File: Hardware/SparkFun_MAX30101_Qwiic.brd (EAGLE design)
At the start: 25.4 x 25.4 mm, 57 parts, among them J1 PTH, J3 QWIIC_RA, J5 QWIIC_RA, Q6 20V/0.2A/8MHz/1.2Ω/1Vth, Q8 20V/0.2A/8MHz/1.2Ω/1Vth, U1 1.8V/100mA, U2 MAX30101

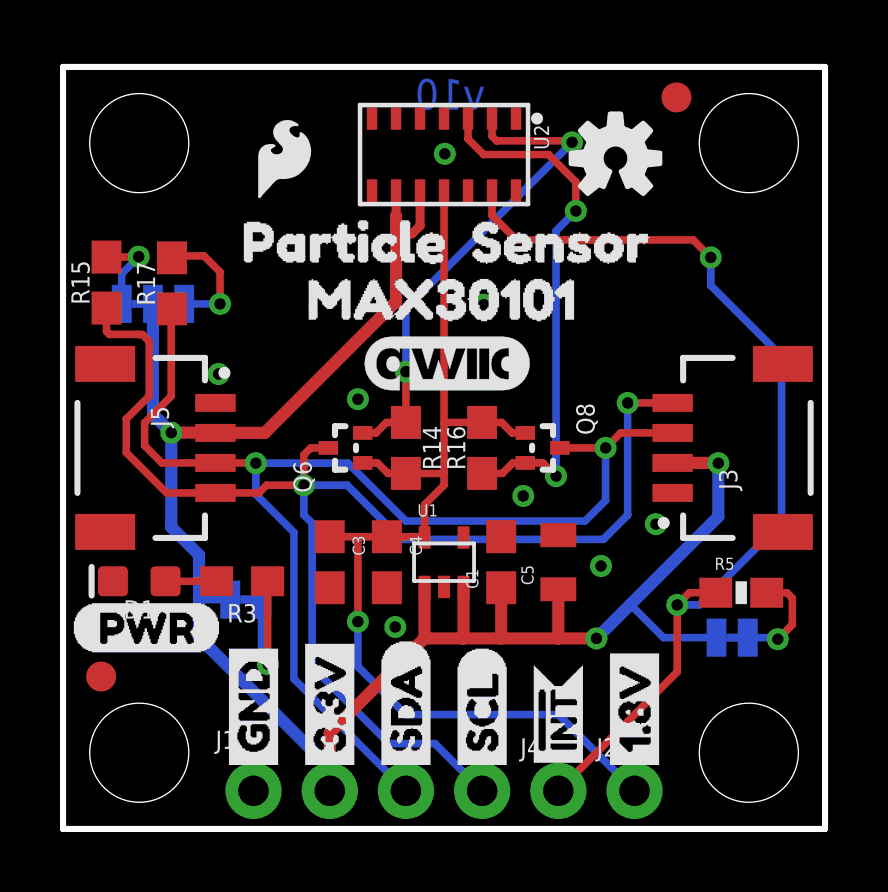
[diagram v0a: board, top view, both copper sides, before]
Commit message: Qwiic logo in SCH and sch cleanup
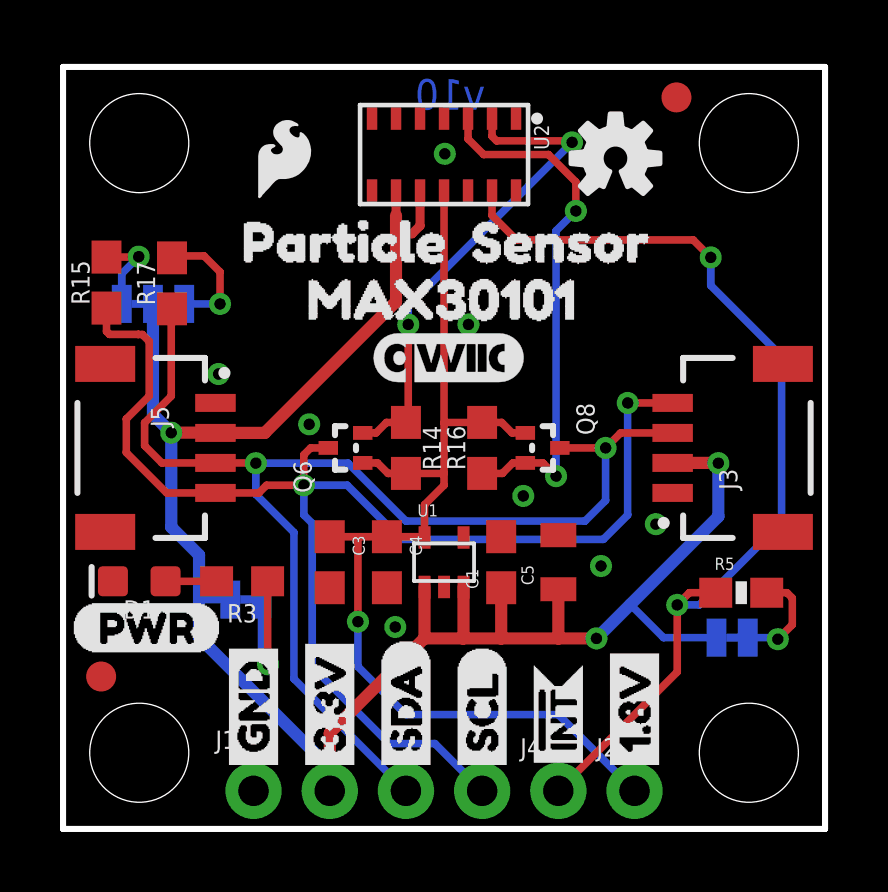
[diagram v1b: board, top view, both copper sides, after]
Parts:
- removed U$15: (no value), SparkFun-Aesthetics:QWIIC_5.5MM
- added LOGO3: QWIIC_LOGO_5MM, SparkFun-Aesthetics:QWIIC_5MM
- moved LOGO1 0.43 mm to (13.3, 17.8)
- moved U$17 0.31 mm to (20.8, 15.9)
- moved U$18 0.30 mm to (13.4, 16.0)
- moved U$24 0.18 mm to (18.7, 14.1)
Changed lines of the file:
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@@
 <grid distance="0.05" unitdist="inch" unit="inch" style="lines" multiple="1" display="yes" altdistance="0.001" altunitdist="inch" altunit="inch"/>
 <layers>
-<layer number="1" name="Top" color="4" fill="1" visible="yes" active="yes"/>
+<layer number="1" name="Top" color="4" fill="1" visible="no" active="yes"/>
 <layer number="2" name="Route2" color="1" fill="3" visible="no" active="no"/>
 <layer number="3" name="Route3" color="4" fill="3" visible="no" active="no"/>
@@
 <layer number="14" name="Route14" color="1" fill="6" visible="no" active="no"/>
 <layer number="15" name="Route15" color="4" fill="6" visible="no" active="no"/>
-<layer number="16" name="Bottom" color="1" fill="1" visible="yes" active="yes"/>
-<layer number="17" name="Pads" color="2" fill="1" visible="yes" active="yes"/>
+<layer number="16" name="Bottom" color="1" fill="1" visible="no" active="yes"/>
+<layer number="17" name="Pads" color="2" fill="1" visible="no" active="yes"/>
 <layer number="18" name="Vias" color="2" fill="1" visible="yes" active="yes"/>
-<layer number="19" name="Unrouted" color="6" fill="1" visible="yes" active="yes"/>
-<layer number="20" name="Dimension" color="15" fill="1" visible="yes" active="yes"/>
-<layer number="21" name="tPlace" color="16" fill="1" visible="yes" active="yes"/>
+<layer number="19" name="Unrouted" color="6" fill="1" visible="no" active="yes"/>
+<layer number="20" name="Dimension" color="15" fill="1" visible="no" active="yes"/>
+<layer number="21" name="tPlace" color="16" fill="1" visible="no" active="yes"/>
 <layer number="22" name="bPlace" color="14" fill="1" visible="yes" active="yes"/>
-<layer number="23" name="tOrigins" color="15" fill="1" visible="yes" active="yes"/>
+<layer number="23" name="tOrigins" color="15" fill="1" visible="no" active="yes"/>
 <layer number="24" name="bOrigins" color="15" fill="1" visible="yes" active="yes"/>
 <layer number="25" name="tNames" color="7" fill="1" visible="no" active="yes"/>
@@
 <layer number="43" name="vRestrict" color="2" fill="10" visible="no" active="yes"/>
 <layer number="44" name="Drills" color="7" fill="1" visible="no" active="yes"/>
-<layer number="45" name="Holes" color="7" fill="1" visible="yes" active="yes"/>
+<layer number="45" name="Holes" color="7" fill="1" visible="no" active="yes"/>
 <layer number="46" name="Milling" color="3" fill="1" visible="no" active="yes"/>
 <layer number="47" name="Measures" color="7" fill="1" visible="no" active="yes"/>
 <layer number="48" name="Document" color="7" fill="1" visible="no" active="yes"/>
-<layer number="49" name="Reference" color="7" fill="1" visible="yes" active="yes"/>
+<layer number="49" name="Reference" color="7" fill="1" visible="no" active="yes"/>
 <layer number="50" name="dxf" color="7" fill="1" visible="no" active="no"/>
-<layer number="51" name="tDocu" color="6" fill="1" visible="yes" active="yes"/>
+<layer number="51" name="tDocu" color="6" fill="1" visible="no" active="yes"/>
 <layer number="52" name="bDocu" color="7" fill="1" visible="no" active="yes"/>
 <layer number="53" name="tGND_GNDA" color="7" fill="9" visible="no" active="no"/>
@@
 <attribute name="VALUE" x="7.747" y="9.906" size="0.4064" layer="27" font="vector" rot="R270"/>
 </element>
-<element name="LOGO1" library="SparkFun-Aesthetics" package="SFE_LOGO_NAME_FLAME_.1" value="SFE_LOGO_NAME_FLAME.1_INCH" x="13.335" y="18.2626" smashed="yes" rot="MR0"/>
+<element name="LOGO1" library="SparkFun-Aesthetics" package="SFE_LOGO_NAME_FLAME_.1" value="SFE_LOGO_NAME_FLAME.1_INCH" x="13.3096" y="17.8308" smashed="yes" rot="MR0"/>
 <element name="LOGO2" library="SparkFun-Aesthetics" package="OSHW-LOGO-S" value="OSHW-LOGOS" x="18.415" y="22.352" smashed="yes"/>
 <element name="U2" library="SparkFun-Sensors" package="OLGA-14" value="MAX30101" x="12.7" y="22.479" smashed="yes" rot="R270">
@@
 <element name="U$20" library="Labels" package="PWR-()-04" value="" x="0.2794" y="6.7056" smashed="yes"/>
 <element name="U$8" library="buzzard_labels (5)" package="LED0" value="" x="8.4582" y="9.398" smashed="yes" rot="MR0"/>
-<element name="U$15" library="SparkFun-Aesthetics" package="QWIIC_5.5MM" value="" x="12.8016" y="15.5194" smashed="yes"/>
 <element name="JP4" library="SparkFun-Jumpers" package="SMT-JUMPER_3_2-NC_TRACE_SILK" package3d_urn="urn:adsk.eagle:package:39289/1" value="I2C PU" x="2.9972" y="17.5006" smashed="yes" rot="MR0">
 <attribute name="NAME" x="2.9972" y="18.6436" size="0.6096" layer="26" font="vector" ratio="20" rot="MR0" align="bottom-center"/>
@@
 <element name="U$6" library="buzzard_labels (8)" package="1#8V1" value="" x="19.05" y="1.651" smashed="yes" rot="MR90"/>
 <element name="U$16" library="SparkFun-Aesthetics" package="QWIIC_5.5MM" value="" x="13.3604" y="12.192" smashed="yes" rot="MR0"/>
-<element name="U$17" library="buzzard_labels (7)" package="PARTICLE1" value="" x="20.828" y="16.2306" smashed="yes" rot="MR0"/>
-<element name="U$18" library="buzzard_labels (7)" package="SENSOR2" value="" x="13.208" y="16.2306" smashed="yes" rot="MR0"/>
-<element name="U$24" library="buzzard_labels (7)" package="MAX301010" value="" x="18.669" y="14.3256" smashed="yes" rot="MR0"/>
+<element name="U$17" library="buzzard_labels (7)" package="PARTICLE1" value="" x="20.8026" y="15.9258" smashed="yes" rot="MR0"/>
+<element name="U$18" library="buzzard_labels (7)" package="SENSOR2" value="" x="13.3604" y="15.9766" smashed="yes" rot="MR0"/>
+<element name="U$24" library="buzzard_labels (7)" package="MAX301010" value="" x="18.7198" y="14.1478" smashed="yes" rot="MR0"/>
+<element name="LOGO3" library="SparkFun-Aesthetics" package="QWIIC_5MM" value="QWIIC_LOGO_5MM" x="12.827" y="15.7226" smashed="yes"/>
 </elements>
 <signals>
@@
 <via x="5.1816" y="15.1638" extent="1-16" drill="0.381"/>
 <via x="12.7254" y="22.5044" extent="1-16" drill="0.381"/>
-<via x="14.0208" y="17.4752" extent="1-16" drill="0.381"/>
-<via x="9.8298" y="14.3256" extent="1-16" drill="0.381"/>
+<via x="13.5128" y="16.8148" extent="1-16" drill="0.381"/>
+<via x="8.2042" y="13.4874" extent="1-16" drill="0.381"/>
 </signal>
 <signal name="SDA">
@@
 <wire x1="10.4314" y1="13.2" x2="9.99" y2="13.2" width="0.254" layer="1"/>
 <wire x1="10.7814" y1="13.55" x2="10.4314" y2="13.2" width="0.254" layer="1"/>
-<wire x1="11.43" y1="13.55" x2="11.43" y2="15.24" width="0.254" layer="1"/>
-<via x="11.43" y="15.24" extent="1-16" drill="0.381"/>
-<wire x1="11.43" y1="15.24" x2="11.43" y2="17.3482" width="0.254" layer="16"/>
-<wire x1="11.43" y1="17.3482" x2="16.9672" y2="22.8854" width="0.254" layer="16"/>
+<wire x1="11.5062" y1="16.8148" x2="11.5062" y2="13.6262" width="0.254" layer="1"/>
+<wire x1="11.43" y1="13.55" x2="11.5062" y2="13.6262" width="0.254" layer="1"/>
+<via x="11.5062" y="16.8148" extent="1-16" drill="0.381"/>
+<wire x1="11.5062" y1="16.8148" x2="11.5062" y2="17.4244" width="0.254" layer="16"/>
+<wire x1="11.5062" y1="17.4244" x2="16.9672" y2="22.8854" width="0.254" layer="16"/>
 <via x="16.9672" y="22.8854" extent="1-16" drill="0.381"/>
 <wire x1="14.3" y1="23.679" x2="14.3" y2="23.0888" width="0.254" layer="1"/>

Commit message: Added I2C address to bottom silk
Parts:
- added U$15: (no value), buzzard_labels (9):ADR#_0X570
- moved LOGO1 2.56 mm to (12.9, 20.3)
- moved U$17 2.29 mm to (20.6, 18.2)
- moved U$18 2.21 mm to (13.3, 18.2)
- moved U$24 1.87 mm to (18.5, 16.0)
- moved U$16 1.84 mm to (13.0, 14.0)
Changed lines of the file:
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@@
 <grid distance="0.05" unitdist="inch" unit="inch" style="lines" multiple="1" display="yes" altdistance="0.001" altunitdist="inch" altunit="inch"/>
 <layers>
-<layer number="1" name="Top" color="4" fill="1" visible="no" active="yes"/>
+<layer number="1" name="Top" color="4" fill="1" visible="yes" active="yes"/>
 <layer number="2" name="Route2" color="1" fill="3" visible="no" active="no"/>
 <layer number="3" name="Route3" color="4" fill="3" visible="no" active="no"/>
@@
 <layer number="14" name="Route14" color="1" fill="6" visible="no" active="no"/>
 <layer number="15" name="Route15" color="4" fill="6" visible="no" active="no"/>
-<layer number="16" name="Bottom" color="1" fill="1" visible="no" active="yes"/>
-<layer number="17" name="Pads" color="2" fill="1" visible="no" active="yes"/>
+<layer number="16" name="Bottom" color="1" fill="1" visible="yes" active="yes"/>
+<layer number="17" name="Pads" color="2" fill="1" visible="yes" active="yes"/>
 <layer number="18" name="Vias" color="2" fill="1" visible="yes" active="yes"/>
-<layer number="19" name="Unrouted" color="6" fill="1" visible="no" active="yes"/>
-<layer number="20" name="Dimension" color="15" fill="1" visible="no" active="yes"/>
-<layer number="21" name="tPlace" color="16" fill="1" visible="no" active="yes"/>
+<layer number="19" name="Unrouted" color="6" fill="1" visible="yes" active="yes"/>
+<layer number="20" name="Dimension" color="15" fill="1" visible="yes" active="yes"/>
+<layer number="21" name="tPlace" color="16" fill="1" visible="yes" active="yes"/>
 <layer number="22" name="bPlace" color="14" fill="1" visible="yes" active="yes"/>
-<layer number="23" name="tOrigins" color="15" fill="1" visible="no" active="yes"/>
+<layer number="23" name="tOrigins" color="15" fill="1" visible="yes" active="yes"/>
 <layer number="24" name="bOrigins" color="15" fill="1" visible="yes" active="yes"/>
 <layer number="25" name="tNames" color="7" fill="1" visible="no" active="yes"/>
@@
 <layer number="43" name="vRestrict" color="2" fill="10" visible="no" active="yes"/>
 <layer number="44" name="Drills" color="7" fill="1" visible="no" active="yes"/>
-<layer number="45" name="Holes" color="7" fill="1" visible="no" active="yes"/>
+<layer number="45" name="Holes" color="7" fill="1" visible="yes" active="yes"/>
 <layer number="46" name="Milling" color="3" fill="1" visible="no" active="yes"/>
 <layer number="47" name="Measures" color="7" fill="1" visible="no" active="yes"/>
 <layer number="48" name="Document" color="7" fill="1" visible="no" active="yes"/>
-<layer number="49" name="Reference" color="7" fill="1" visible="no" active="yes"/>
+<layer number="49" name="Reference" color="7" fill="1" visible="yes" active="yes"/>
 <layer number="50" name="dxf" color="7" fill="1" visible="no" active="no"/>
-<layer number="51" name="tDocu" color="6" fill="1" visible="no" active="yes"/>
+<layer number="51" name="tDocu" color="6" fill="1" visible="yes" active="yes"/>
 <layer number="52" name="bDocu" color="7" fill="1" visible="no" active="yes"/>
 <layer number="53" name="tGND_GNDA" color="7" fill="9" visible="no" active="no"/>
@@
 <attribute name="VALUE" x="7.747" y="9.906" size="0.4064" layer="27" font="vector" rot="R270"/>
 </element>
-<element name="LOGO1" library="SparkFun-Aesthetics" package="SFE_LOGO_NAME_FLAME_.1" value="SFE_LOGO_NAME_FLAME.1_INCH" x="13.3096" y="17.8308" smashed="yes" rot="MR0"/>
+<element name="LOGO1" library="SparkFun-Aesthetics" package="SFE_LOGO_NAME_FLAME_.1" value="SFE_LOGO_NAME_FLAME.1_INCH" x="12.8524" y="20.3454" smashed="yes" rot="MR0"/>
 <element name="LOGO2" library="SparkFun-Aesthetics" package="OSHW-LOGO-S" value="OSHW-LOGOS" x="18.415" y="22.352" smashed="yes"/>
 <element name="U2" library="SparkFun-Sensors" package="OLGA-14" value="MAX30101" x="12.7" y="22.479" smashed="yes" rot="R270">
@@
 <element name="U$5" library="buzzard_labels (8)" package="1#8V1" value="" x="19.05" y="1.651" smashed="yes" rot="R90"/>
 <element name="U$6" library="buzzard_labels (8)" package="1#8V1" value="" x="19.05" y="1.651" smashed="yes" rot="MR90"/>
-<element name="U$16" library="SparkFun-Aesthetics" package="QWIIC_5.5MM" value="" x="13.3604" y="12.192" smashed="yes" rot="MR0"/>
-<element name="U$17" library="buzzard_labels (7)" package="PARTICLE1" value="" x="20.8026" y="15.9258" smashed="yes" rot="MR0"/>
-<element name="U$18" library="buzzard_labels (7)" package="SENSOR2" value="" x="13.3604" y="15.9766" smashed="yes" rot="MR0"/>
-<element name="U$24" library="buzzard_labels (7)" package="MAX301010" value="" x="18.7198" y="14.1478" smashed="yes" rot="MR0"/>
+<element name="U$16" library="SparkFun-Aesthetics" package="QWIIC_5.5MM" value="" x="13.0048" y="13.9954" smashed="yes" rot="MR0"/>
+<element name="U$17" library="buzzard_labels (7)" package="PARTICLE1" value="" x="20.6248" y="18.2118" smashed="yes" rot="MR0"/>
+<element name="U$18" library="buzzard_labels (7)" package="SENSOR2" value="" x="13.335" y="18.1864" smashed="yes" rot="MR0"/>
+<element name="U$24" library="buzzard_labels (7)" package="MAX301010" value="" x="18.4658" y="16.002" smashed="yes" rot="MR0"/>
 <element name="LOGO3" library="SparkFun-Aesthetics" package="QWIIC_5MM" value="QWIIC_LOGO_5MM" x="12.827" y="15.7226" smashed="yes"/>
+<element name="U$15" library="buzzard_labels (9)" package="ADR#_0X570" value="" x="17.2212" y="12.1412" smashed="yes" rot="MR0"/>
 </elements>
 <signals>

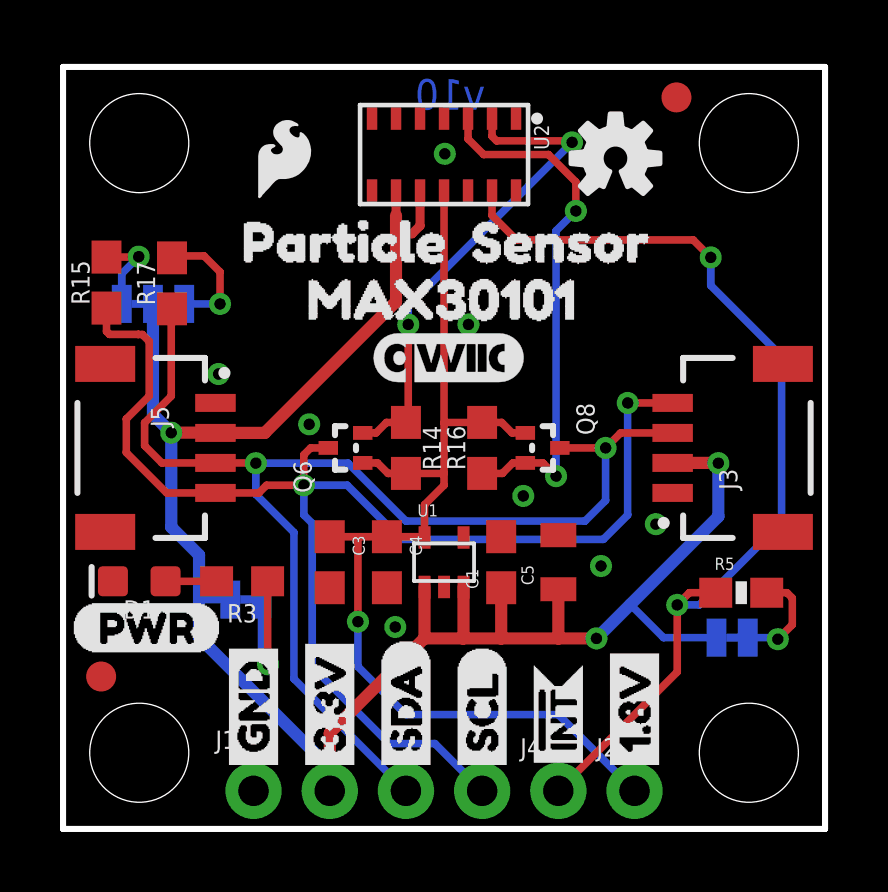
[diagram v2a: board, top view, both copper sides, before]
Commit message: Added 5V step up for green LED and review changes
-Added in 5V step up circuit to provide 5V for Green LED
-Add fids to bottom
-move power led label to text only
-3.3V trace could loose a via and then stitch up gnd with more vias
-move IC device to the true MAX30105 in the library.
-flip v10 in copper to read "along" the bottom.
-remove JP labels to jumpers, since they already have the names of their purposes.
-input voltage range in sch.
-Change 1.8V label flag to an output
-add typical current consuption for the sensor in the schematic near the IC symbol
-Move QWIIC lozenge to right over by the qwiic connector.
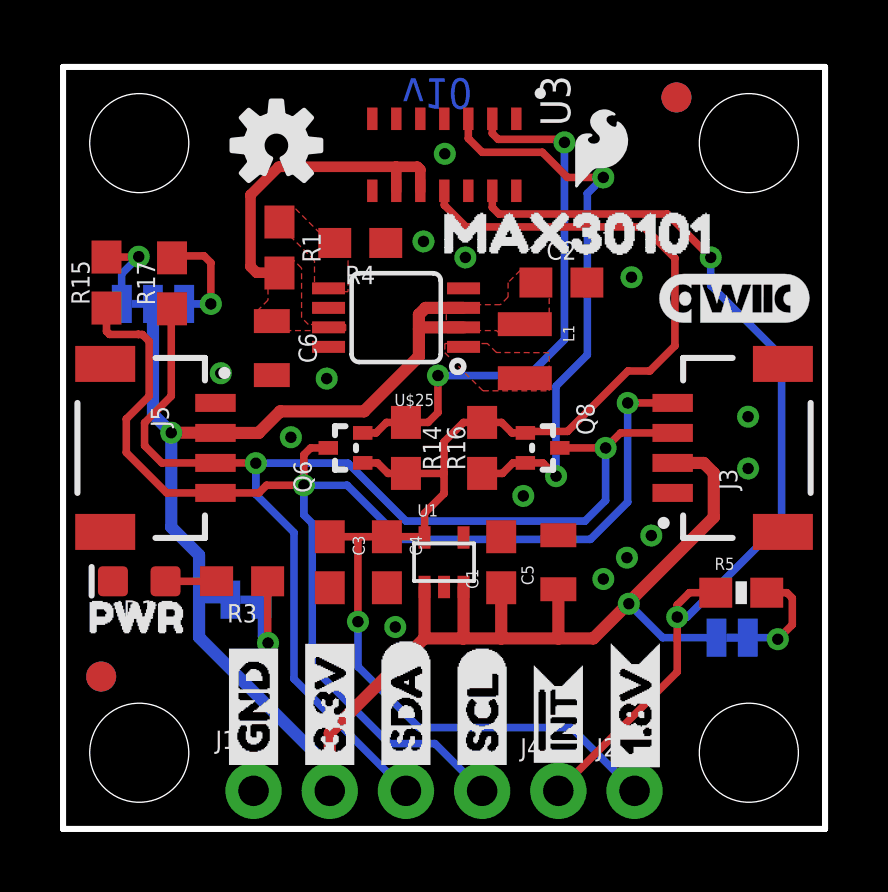
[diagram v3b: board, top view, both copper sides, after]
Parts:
- removed U$1: (no value), buzzard_labels (7):PARTICLE1
- removed U$2: (no value), buzzard_labels (7):SENSOR2
- removed U$5, U$6: (no value), buzzard_labels (8):1#8V1
- removed U2: MAX30101, SparkFun-Sensors:OLGA-14
- added C2: 10uF, SparkFun-Capacitors:0603
- added C6: 22uF, SparkFun-Capacitors:0805
- added FID3, FID4: FIDUCIAL1X2, SparkFun-Aesthetics:FIDUCIAL-1X2
- added L1: 2.2μH, SparkFun-Coils:0806
- added R1: 750K, SparkFun-Resistors:0603
- added R4: 100k, SparkFun-Resistors:0603
- added U$25: PAM2401, SparkFun-IC-Power:MSOP8
- added U$26: (no value), SparkFun-Buzzard:PWR_TO
- added U$27: (no value), buzzard_labels (10):1#8V0
- added U3: MAX30101EFD, SparkFun-IC-Special-Function:14_PIN_OESIP
- R14, R15, R16, R17, R3: device SparkFun-Resistors:0603 -> SparkFun-Resistors:0603@1
- U$20: device Labels:PWR-()-04 -> buzzard_labels (10):1#8V0
- moved U$20 19.5 mm to (19.1, 1.57), turned to 90 degrees
- moved LOGO2 11.3 mm to (7.11, 22.8)
- moved LOGO4 10.6 mm to (17.9, 22.7)
- moved LOGO3 9.73 mm to (22.4, 17.7)
- moved U$4 5.03 mm to (11.5, 19.9)
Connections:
- new net 5V: C6.1, R1.2, U$25.7, U3.P10, U3.P9
- new net N$2: R1.1, R4.2, U$25.5
- new net N$3: L1.2, U$25.1
- net !INT: now also U3.P13; no longer U2.13
- net 1.8V: now also U3.P11; no longer U2.11
- net 3.3V: now also C2.1, L1.1, U$25.2, U$25.3; no longer U2.10, U2.9
- net GND: now also C2.2, C6.2, R4.1, U$25.4, U$25.8, U3.P12, U3.P4; no longer U2.12, U2.4
- net LV_SCL: now also U3.P2; no longer U2.2
- net LV_SDA: now also U3.P3; no longer U2.3
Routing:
- net 5V: track 0.00 -> 11.0 mm
- net 1.8V: track 36.0 -> 45.9 mm
- net LV_SCL: track 16.6 -> 18.3 mm
- net 3.3V: track 66.1 -> 64.4 mm, vias 3 -> 2
- net N$8: track 5.02 -> 3.60 mm
- net LV_SDA: track 17.7 -> 19.1 mm
- added copper zone on layer 1, net 3.3V
- added copper zone on layer 1, net 5V
- added copper zone on layer 1, net N$2
- added copper zone on layer 1, net N$3
